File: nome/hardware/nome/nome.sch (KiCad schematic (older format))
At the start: 47 parts, among them J1 Audio-Jack-3_2Switches, J2 JTAG_Conn_01x05_Male, SW1 SW_SPST, SW2 Rotary_Encoder_Switch, U1 LM1117-1.8, U2 LM1117-3.3, U3 AS1115, U4 STMF411CEU6, U5 LTC-4727JS, U6 CS43L22

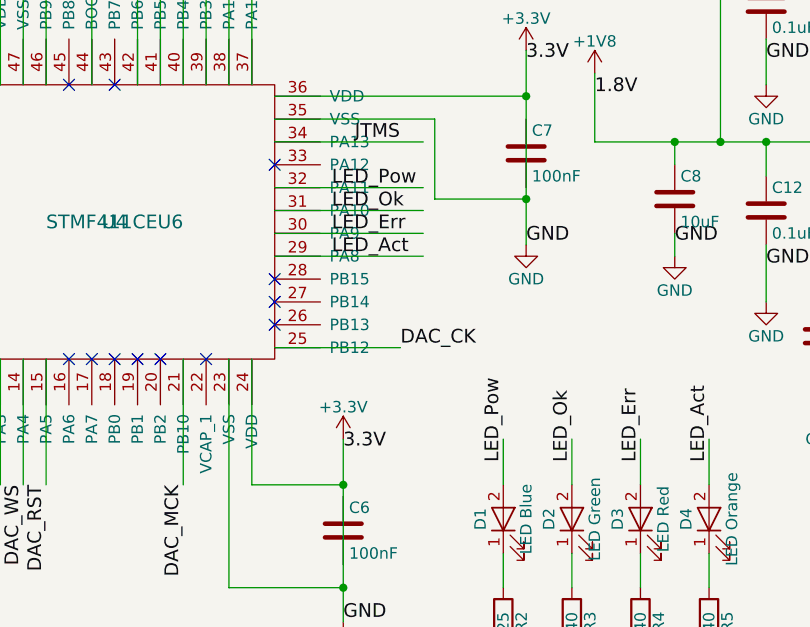
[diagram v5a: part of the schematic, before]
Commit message: Tie power LED to 3.3v
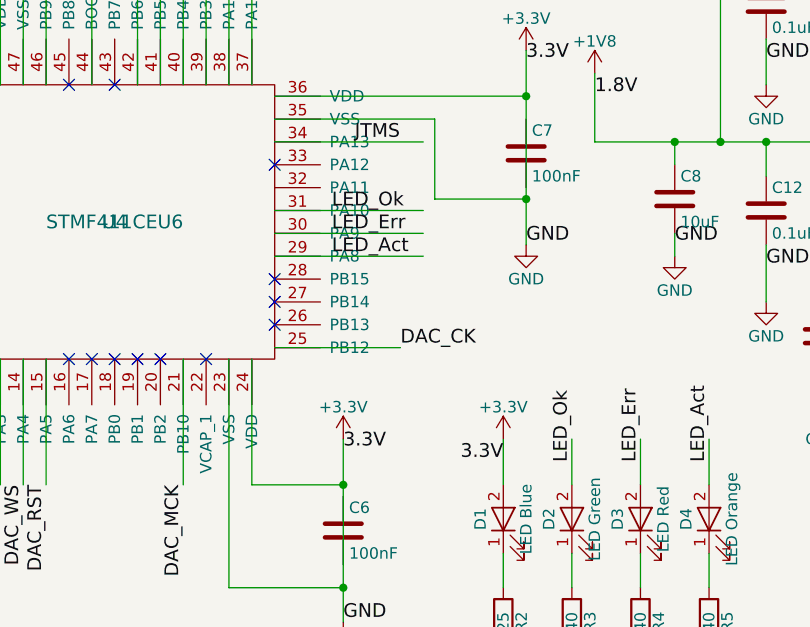
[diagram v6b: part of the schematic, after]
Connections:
- net labels removed: LED_Pow
- wire segments 210 -> 209
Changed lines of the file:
@@
 	0    -1   -1   0
 $EndComp
-Text Label 5550 5300 1    60   ~ 0
-LED_Pow
 Text Label 5850 5300 1    60   ~ 0
 LED_Ok
@@
 Text Label 6450 5300 1    60   ~ 0
 LED_Act
-Text Label 4800 4100 0    60   ~ 0
-LED_Pow
 Text Label 4800 4200 0    60   ~ 0
 LED_Ok
@@
 	6450 5400 6450 5200
 Wire Wire Line
-	4550 4100 5200 4100
-Wire Wire Line
 	4550 4200 5200 4200
 Wire Wire Line
@@
 Text Label 4150 3150 1    60   ~ 0
 JTRST
+$Comp
+L +3.3V #PWR?
+U 1 1 59EDA31D
+P 5550 5200
+F 0 "#PWR?" H 5550 5050 50  0001 C CNN
+F 1 "+3.3V" H 5550 5340 50  0000 C CNN
+F 2 "" H 5550 5200 50  0001 C CNN
+F 3 "" H 5550 5200 50  0001 C CNN
+	1    5550 5200
+	1    0    0    -1
+$EndComp
+Text Label 5550 5300 2    60   ~ 0
+3.3V
 $EndSCHEMATC

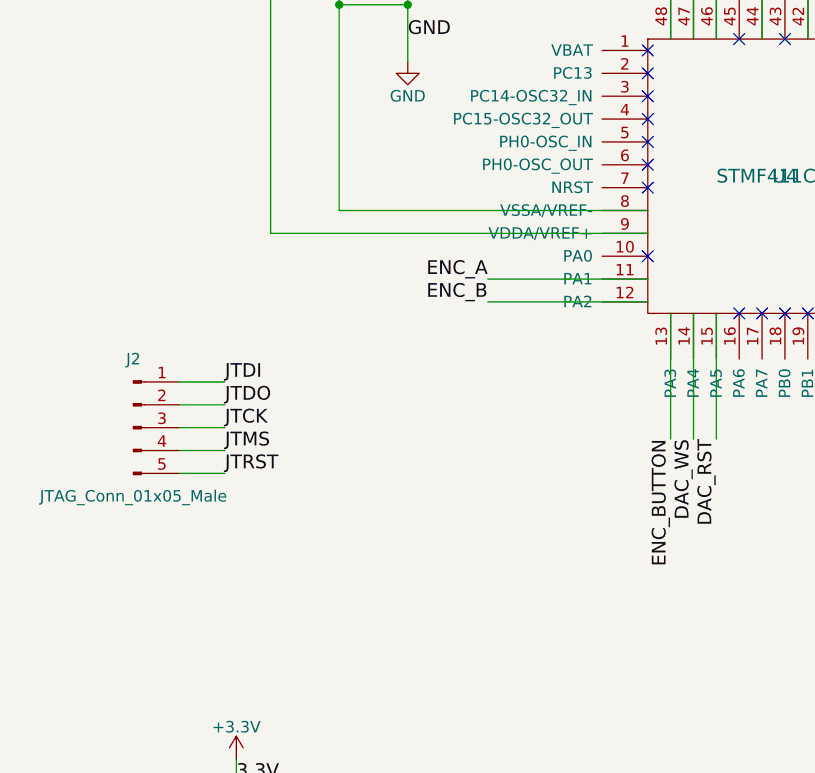
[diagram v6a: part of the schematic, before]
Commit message: Switch to standard 10-pin ARM cortex JTAG/SWD connector
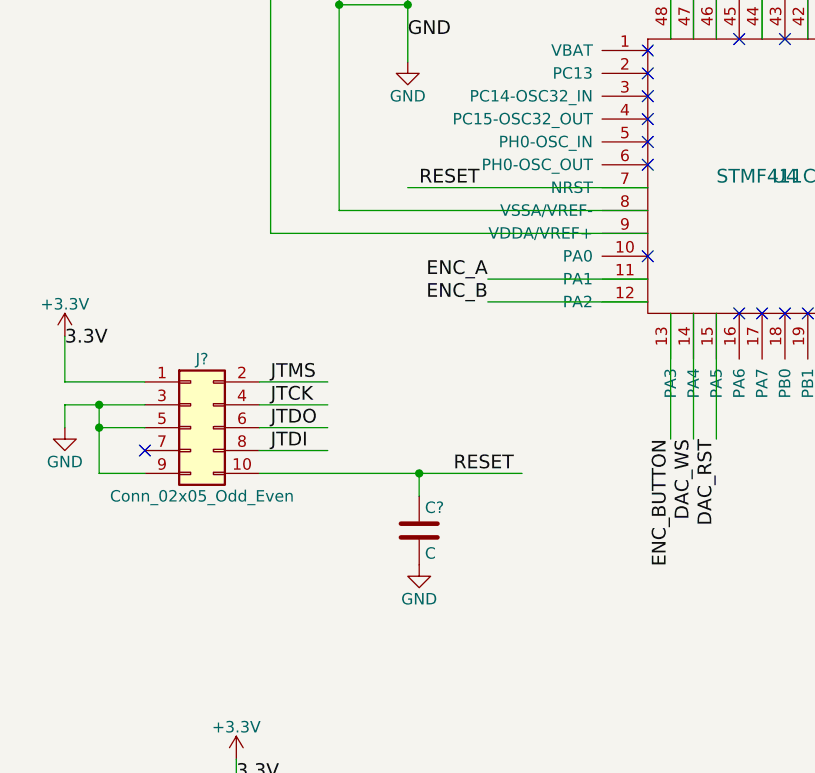
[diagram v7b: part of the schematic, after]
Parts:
- removed J2: JTAG_Conn_01x05_Male, symbol Conn_01x05_Male
- added C?: C, symbol C
- added J?: Conn_02x05_Odd_Even, symbol Conn_02x05_Odd_Even
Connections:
- net labels added: RESET
- wire segments 209 -> 218
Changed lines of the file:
@@
 NoConn ~ 3250 4100
 NoConn ~ 3250 4200
-NoConn ~ 3250 4300
 NoConn ~ 3250 4600
 NoConn ~ 3650 4850
@@
 	-1   0    0    1
 $EndComp
-$Comp
-L Conn_01x05_Male J2
-U 1 1 59ED75CA
-P 1000 5350
-F 0 "J2" H 1000 5650 50  0000 C CNN
-F 1 "JTAG_Conn_01x05_Male" H 1000 5050 50  0000 C CNN
-F 2 "" H 1000 5350 50  0001 C CNN
-F 3 "" H 1000 5350 50  0001 C CNN
-	1    1000 5350
-	1    0    0    -1
-$EndComp
-Wire Wire Line
-	1200 5150 1400 5150
-Text Label 1400 5150 0    60   ~ 0
-JTDI
-Wire Wire Line
-	1200 5250 1400 5250
-Text Label 1400 5250 0    60   ~ 0
-JTDO
-Wire Wire Line
-	1200 5350 1400 5350
-Text Label 1400 5350 0    60   ~ 0
-JTCK
-Wire Wire Line
-	1200 5450 1400 5450
-Text Label 1400 5450 0    60   ~ 0
-JTMS
-Wire Wire Line
-	1200 5550 1400 5550
-Text Label 1400 5550 0    60   ~ 0
-JTRST
 Wire Wire Line
 	4550 3900 5200 3900
@@
 Text Label 5550 5300 2    60   ~ 0
 3.3V
+$Comp
+L Conn_02x05_Odd_Even J?
+U 1 1 59EDA6EA
+P 1250 5350
+F 0 "J?" H 1300 5650 50  0000 C CNN
+F 1 "Conn_02x05_Odd_Even" H 1300 5050 50  0000 C CNN
+F 2 "" H 1250 5350 50  0001 C CNN
+F 3 "" H 1250 5350 50  0001 C CNN
+	1    1250 5350
+	1    0    0    -1
+$EndComp
+Wire Wire Line
+	1550 5150 1850 5150
+Text Label 1600 5150 0    60   ~ 0
+JTMS
+Wire Wire Line
+	1550 5250 1850 5250
+Text Label 1600 5250 0    60   ~ 0
+JTCK
+Wire Wire Line
+	1550 5350 1850 5350
+Text Label 1600 5350 0    60   ~ 0
+JTDO
+Wire Wire Line
+	1550 5450 1850 5450
+Text Label 1600 5450 0    60   ~ 0
+JTDI
+Wire Wire Line
+	1550 5550 2700 5550
+Wire Wire Line
+	1050 5350 850  5350
+Wire Wire Line
+	850  5250 850  5550
+Wire Wire Line
+	700  5250 1050 5250
+Wire Wire Line
+	700  5250 700  5350
+Connection ~ 850  5250
+$Comp
+L GND #PWR?
+U 1 1 59EDB933
+P 700 5350
+F 0 "#PWR?" H 700 5100 50  0001 C CNN
+F 1 "GND" H 700 5200 50  0000 C CNN
+F 2 "" H 700 5350 50  0001 C CNN
+F 3 "" H 700 5350 50  0001 C CNN
+	1    700  5350
+	1    0    0    -1
+$EndComp
+NoConn ~ 1050 5450
+Wire Wire Line
+	850  5550 1050 5550
+Connection ~ 850  5350
+Wire Wire Line
+	1050 5150 700  5150
+Wire Wire Line
+	700  5150 700  4950
+$Comp
+L +3.3V #PWR?
+U 1 1 59EDBC98
+P 700 4950
+F 0 "#PWR?" H 700 4800 50  0001 C CNN
+F 1 "+3.3V" H 700 5090 50  0000 C CNN
+F 2 "" H 700 4950 50  0001 C CNN
+F 3 "" H 700 4950 50  0001 C CNN
+	1    700  4950
+	1    0    0    -1
+$EndComp
+Text Label 700  5000 0    60   ~ 0
+3.3V
+$Comp
+L GND #PWR?
+U 1 1 59EDC1EB
+P 2250 5950
+F 0 "#PWR?" H 2250 5700 50  0001 C CNN
+F 1 "GND" H 2250 5800 50  0000 C CNN
+F 2 "" H 2250 5950 50  0001 C CNN
+F 3 "" H 2250 5950 50  0001 C CNN
+	1    2250 5950
+	1    0    0    -1
+$EndComp
+$Comp
+L C C?
+U 1 1 59EDC25D
+P 2250 5800
+F 0 "C?" H 2275 5900 50  0000 L CNN
+F 1 "C" H 2275 5700 50  0000 L CNN
+F 2 "" H 2288 5650 50  0001 C CNN
+F 3 "" H 2250 5800 50  0001 C CNN
+	1    2250 5800
+	1    0    0    -1
+$EndComp
+Wire Wire Line
+	2250 5550 2250 5650
+Connection ~ 2250 5550
+Text Label 2400 5550 0    60   ~ 0
+RESET
+Wire Wire Line
+	3250 4300 2200 4300
+Text Label 2250 4300 0    60   ~ 0
+RESET
 $EndSCHEMATC

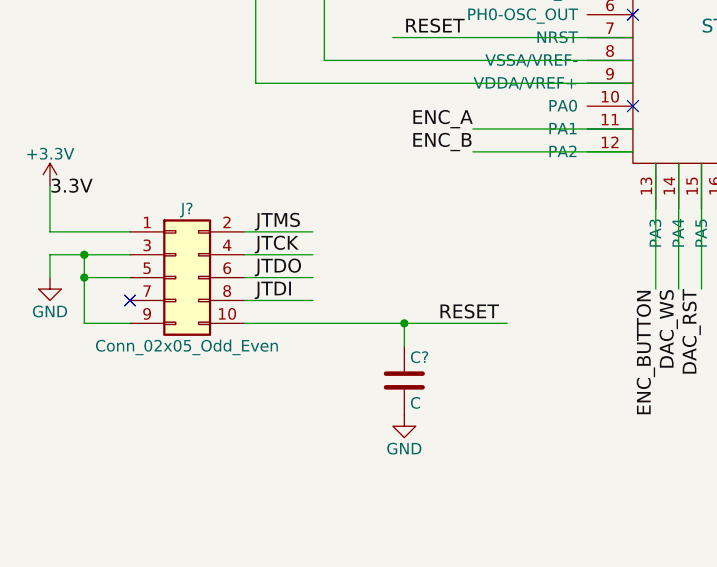
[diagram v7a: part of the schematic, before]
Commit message: Redo annotations
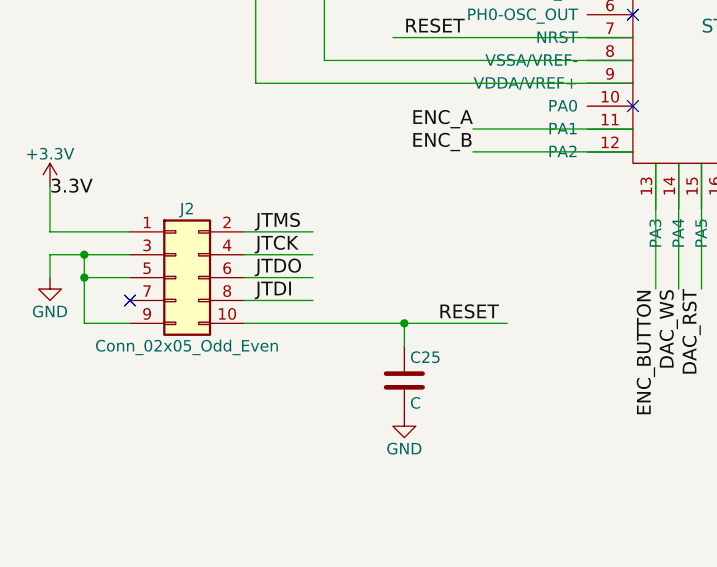
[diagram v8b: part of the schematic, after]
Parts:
- gave numbers to parts that had none: 2
